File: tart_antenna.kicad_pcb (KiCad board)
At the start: 6 copper layers, 99.1 x 66 mm, 10 parts, among them J1 RFShield_OnePiece, J2 Conn_Coaxial, U1 5400BL15B050, U2 BGU7005

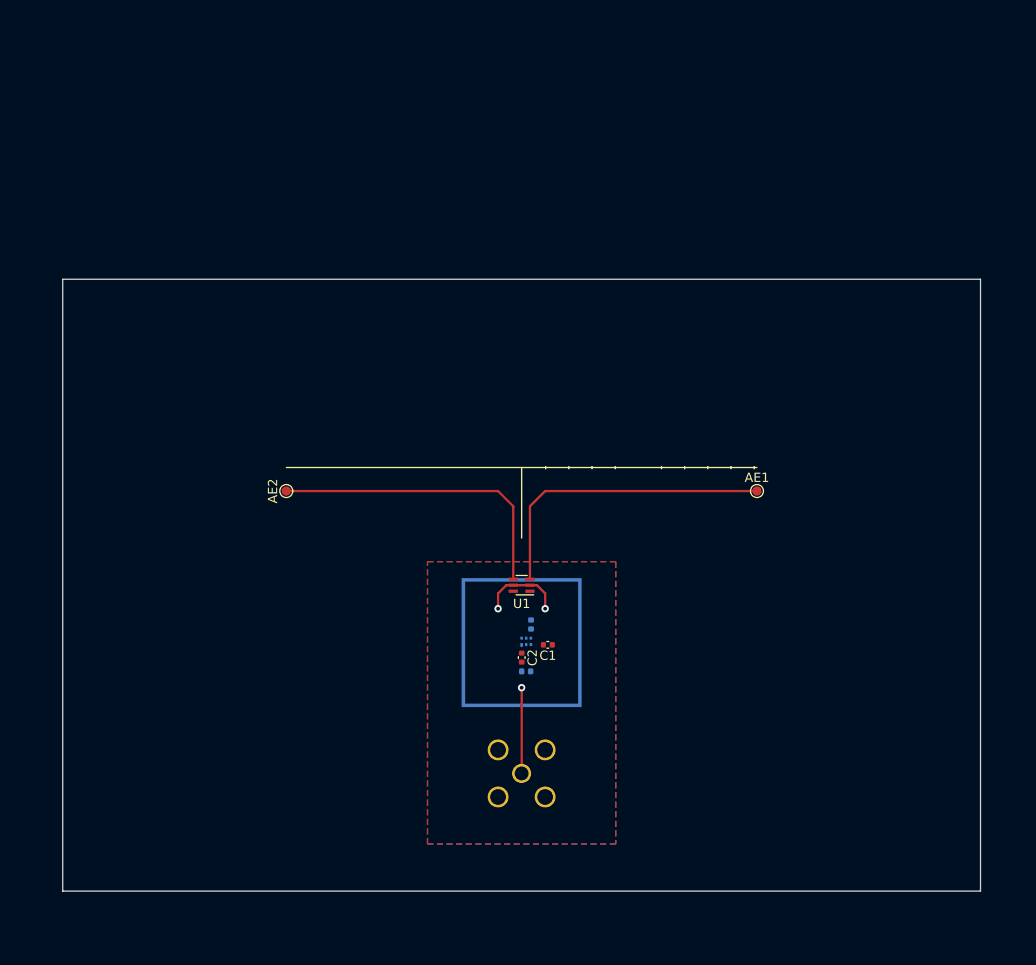
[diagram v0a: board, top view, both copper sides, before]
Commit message: Added round background
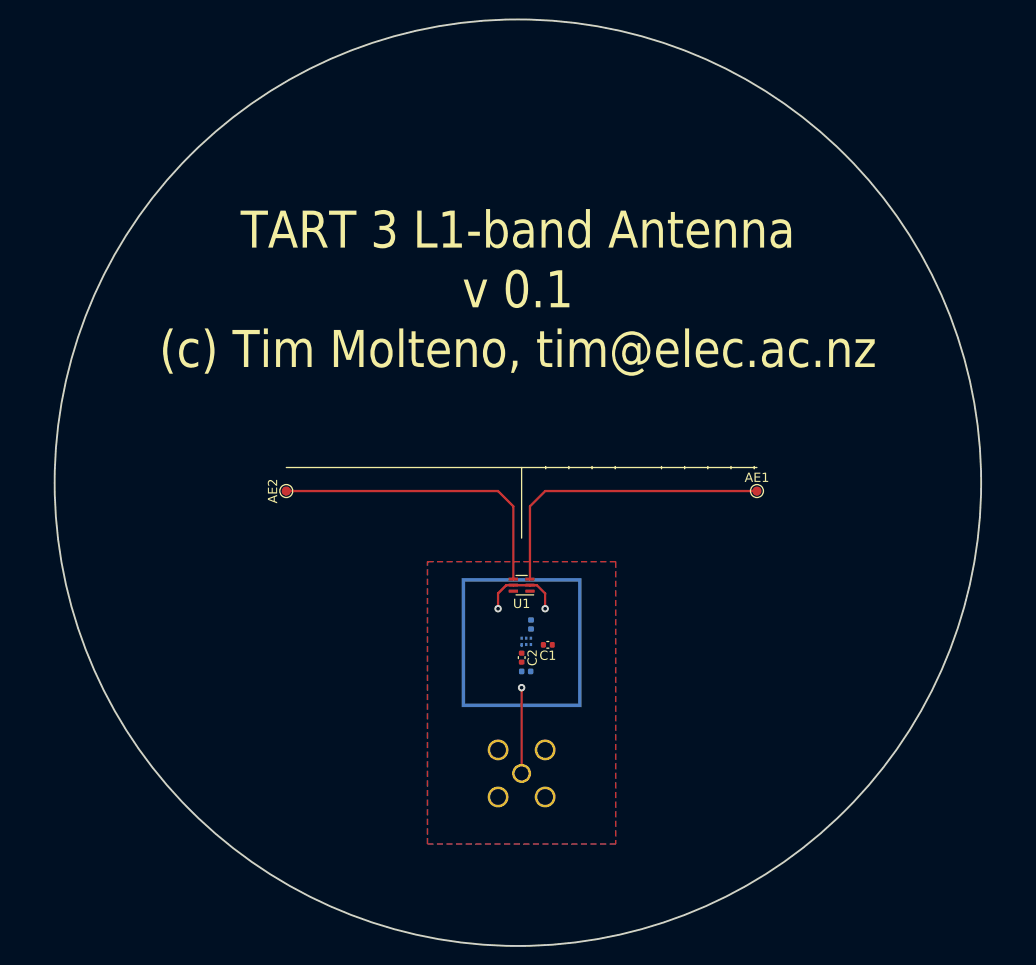
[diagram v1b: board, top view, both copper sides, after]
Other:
- board size 99.1 x 66 mm -> 100 x 100 mm
- board text added: "TART 3 L1-band Antenna v 0.1 (c) Tim Molteno, tim@elec.ac.nz"
